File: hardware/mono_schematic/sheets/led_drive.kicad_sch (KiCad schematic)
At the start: 31 parts

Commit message: mono_electronics v11b: TLV75733P 1A AON LDO, 22uF ESP32 bulk, LED_EN RC glitch filter, J_USB value, refs end in digit; schematic regenerated (ERC 0, 0 diffs)
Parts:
- removed C_BUF_V, C_DECA_V, C_DECB_V, C_LED1_V, C_LED2_V, C_XLAT_A, C_XLAT_B: 100n, mono_electronics:C_0402_1005Metric, symbol mono_parts:100n_C_0402_1005Metric_2
- removed J_COL: FFC_40P_050_COL, mono_electronics:FFC_40P_050_COL, symbol mono_parts:FFC_40P_050_COL_FFC_40P_050_COL_40
- removed R_CLK_PD, R_LE_PD, R_SDI_PD: 100k, mono_electronics:R_0402_1005Metric, symbol mono_parts:100k_R_0402_1005Metric_2
- removed R_CLK_SER, R_LE_SER, R_SDI_SER: 22R, mono_electronics:R_0402_1005Metric, symbol mono_parts:22R_R_0402_1005Metric_2
- removed R_ENA, R_ENB, R_OE_PU, R_OE_YPU: 47k, mono_electronics:R_0402_1005Metric, symbol mono_parts:47k_R_0402_1005Metric_2
- removed R_XOE: 10k, mono_electronics:R_0402_1005Metric, symbol mono_parts:10k_R_0402_1005Metric_2
- removed U_DEC_A, U_DEC_B: 74HC154, mono_electronics:TSSOP-24_4.4x7.8mm_P0.65mm, symbol mono_parts:74HC154_TSSOP-24_4.4x7.8mm_P0.65mm_24
- removed U_LED_BUF: SN74LV125A, mono_electronics:TSSOP-14_4.4x5mm_P0.65mm, symbol mono_parts:SN74LV125A_TSSOP-14_4.4x5mm_P0.65mm_14
- removed U_ROW_XLAT: SN74LVC8T245RHLR, mono_electronics:Texas_RHL0024A_VQFN-24-1EP_3.5x5.5mm_P0.5mm_EP2.05x4.05mm, symbol mono_parts:SN74LVC8T245RHLR_Texas_RHL0024A_VQFN-24-1EP_3.5x5.5mm_P0.5mm_EP2.05x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
- added C_BUF_V1, C_DECA_V1, C_DECB_V1, C_LED1_V1, C_LED2_V1, C_XLAT_A1, C_XLAT_B1: 100n, mono_electronics:C_0402_1005Metric, symbol mono_parts:100n_C_0402_1005Metric_2
- added J_COL1: FFC_40P_050_COL, mono_electronics:FFC_40P_050_COL, symbol mono_parts:FFC_40P_050_COL_FFC_40P_050_COL_40
- added R_CLK_PD1, R_EN_PD1, R_EN_SER1, R_LE_PD1, R_SDI_PD1: 100k, mono_electronics:R_0402_1005Metric, symbol mono_parts:100k_R_0402_1005Metric_2
- added R_CLK_SER1, R_LE_SER1, R_SDI_SER1: 22R, mono_electronics:R_0402_1005Metric, symbol mono_parts:22R_R_0402_1005Metric_2
- added R_ENA1, R_ENB1, R_OE_PU1, R_OE_YPU1: 47k, mono_electronics:R_0402_1005Metric, symbol mono_parts:47k_R_0402_1005Metric_2
- added R_XOE1: 10k, mono_electronics:R_0402_1005Metric, symbol mono_parts:10k_R_0402_1005Metric_2
- added U_DEC_A1, U_DEC_B1: 74HC154, mono_electronics:TSSOP-24_4.4x7.8mm_P0.65mm, symbol mono_parts:74HC154_TSSOP-24_4.4x7.8mm_P0.65mm_24
- added U_LED_BUF1: SN74LV125A, mono_electronics:TSSOP-14_4.4x5mm_P0.65mm, symbol mono_parts:SN74LV125A_TSSOP-14_4.4x5mm_P0.65mm_14
- added U_LED_LOGIC1: TPS22917, mono_electronics:SOT-23-6, symbol mono_parts:TPS22917_SOT-23-6_5
- added U_LED_PWR1: TPS63802DLAR, mono_electronics:TDFN-10-1EP_2x3mm_P0.5mm_EP0.9x2mm, symbol mono_parts:TPS63802DLAR_TDFN-10-1EP_2x3mm_P0.5mm_EP0.9x2mm_10
- added U_ROW_XLAT1: SN74LVC8T245RHLR, mono_electronics:Texas_RHL0024A_VQFN-24-1EP_3.5x5.5mm_P0.5mm_EP2.05x4.05mm, symbol mono_parts:SN74LVC8T245RHLR_Texas_RHL0024A_VQFN-24-1EP_3.5x5.5mm_P0.5mm_EP2.05x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
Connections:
- net AON_3V3: now also C_XLAT_A1.1, R_OE_PU1.2, R_XOE1.1, U_LED_LOGIC1.1 (AON_3V3), U_ROW_XLAT1.1 (AON_3V3), U_ROW_XLAT1.2 (AON_3V3)
- net COL_01: now also J_COL1.1 (COL_01)
- net COL_02: now also J_COL1.2 (COL_02)
- net COL_03: now also J_COL1.3 (COL_03)
- net COL_04: now also J_COL1.4 (COL_04)
- net COL_05: now also J_COL1.5 (COL_05)
- net COL_06: now also J_COL1.6 (COL_06)
- net COL_07: now also J_COL1.7 (COL_07)
- net COL_08: now also J_COL1.8 (COL_08)
- net COL_09: now also J_COL1.9 (COL_09)
- net COL_10: now also J_COL1.10 (COL_10)
- net COL_11: now also J_COL1.11 (COL_11)
- net COL_12: now also J_COL1.12 (COL_12)
- net COL_13: now also J_COL1.13 (COL_13)
- net COL_14: now also J_COL1.14 (COL_14)
- net COL_15: now also J_COL1.15 (COL_15)
- net COL_16: now also J_COL1.16 (COL_16)
- net COL_17: now also J_COL1.17 (COL_17)
- net COL_18: now also J_COL1.18 (COL_18)
- net COL_19: now also J_COL1.19 (COL_19)
- net COL_20: now also J_COL1.20 (COL_20)
- net COL_21: now also J_COL1.21 (COL_21)
- net COL_22: now also J_COL1.22 (COL_22)
- net COL_23: now also J_COL1.23 (COL_23)
- net COL_24: now also J_COL1.24 (COL_24)
- net COL_25: now also J_COL1.25 (COL_25)
- net COL_26: now also J_COL1.26 (COL_26)
- net COL_27: now also J_COL1.27 (COL_27)
- net COL_28: now also J_COL1.28 (COL_28)
- net COL_29: now also J_COL1.29 (COL_29)
- net COL_30: now also J_COL1.30 (COL_30)
- net COL_31: now also J_COL1.31 (COL_31)
- net COL_32: now also J_COL1.32 (COL_32)
- net DEC_A_EN_N: now also U_ROW_XLAT1.7 (DEC_A_EN_N)
- net DEC_A_EN_N_4V: now also R_ENA1.1, U_DEC_A1.18 (DEC_A_EN_N_4V), U_ROW_XLAT1.17 (DEC_A_EN_N_4V)
- net DEC_B_EN_N: now also U_ROW_XLAT1.8 (DEC_B_EN_N)
- net DEC_B_EN_N_4V: now also R_ENB1.1, U_DEC_B1.18 (DEC_A_EN_N_4V), U_ROW_XLAT1.16 (DEC_B_EN_N_4V)
- net GND: now also C_BUF_V1.2, C_DECA_V1.2, C_DECB_V1.2, C_LED1_V1.2, C_LED2_V1.2, C_XLAT_A1.2, C_XLAT_B1.2, R_CLK_PD1.2, R_EN_PD1.2, R_LE_PD1.2, R_SDI_PD1.2, U_DEC_A1.12 (GND), U_DEC_A1.19 (GND), U_DEC_B1.12 (GND), U_DEC_B1.19 (GND), U_LED_BUF1.1 (GND), U_LED_BUF1.10 (GND), U_LED_BUF1.13 (GND), U_LED_BUF1.4 (GND), U_LED_BUF1.7 (GND), U_LED_LOGIC1.2 (GND), U_LED_PWR1.11 (GND), U_LED_PWR1.2 (GND), U_LED_PWR1.3 (GND), U_LED_PWR1.8 (GND), U_ROW_XLAT1.10 (GND), U_ROW_XLAT1.11 (GND), U_ROW_XLAT1.12 (GND), U_ROW_XLAT1.13 (GND), U_ROW_XLAT1.25 (GND), U_ROW_XLAT1.9 (GND)
- net LED_4V1: now also C_DECA_V1.1, C_DECB_V1.1, C_XLAT_B1.1, R_ENA1.2, R_ENB1.2, U_DEC_A1.24 (LED_4V1), U_DEC_B1.24 (LED_4V1), U_LED_PWR1.6 (LED_4V1), U_ROW_XLAT1.23 (LED_4V1), U_ROW_XLAT1.24 (LED_4V1)
- net LED_CLK: now also R_CLK_PD1.1, U_LED_BUF1.2 (LED_CLK)
- net LED_CLK_PRE: now also R_CLK_SER1.1, U_LED_BUF1.3 (LED_CLK_PRE)
- net LED_CLK_Y: now also R_CLK_SER1.2
- net LED_LE: now also R_LE_PD1.1, U_LED_BUF1.9 (LED_LE)
- net LED_LE_PRE: now also R_LE_SER1.1, U_LED_BUF1.8 (LED_LE_PRE)
- net LED_LE_Y: now also R_LE_SER1.2
- net LED_LOGIC_3V3: now also C_BUF_V1.1, C_LED1_V1.1, C_LED2_V1.1, R_OE_YPU1.2, U_LED_BUF1.14 (LED_LOGIC_3V3), U_LED_LOGIC1.6 (LED_LOGIC_3V3)
- net LED_OE_N: now also R_OE_PU1.1, U_LED_BUF1.12 (LED_OE_N)
- net LED_OE_Y: now also R_OE_YPU1.1, U_LED_BUF1.11 (LED_OE_Y)
- net LED_SDI: now also R_SDI_PD1.1, U_LED_BUF1.5 (LED_SDI)
- net LED_SDI_PRE: now also R_SDI_SER1.1, U_LED_BUF1.6 (LED_SDI_PRE)
- net LED_SDI_Y: now also R_SDI_SER1.2
- net ROW_01_Y: now also U_DEC_A1.1 (ROW_01_Y)
- net ROW_02_Y: now also U_DEC_A1.2 (ROW_02_Y)
- net ROW_03_Y: now also U_DEC_A1.3 (ROW_03_Y)
- net ROW_04_Y: now also U_DEC_A1.4 (ROW_04_Y)
- net ROW_05_Y: now also U_DEC_A1.5 (ROW_05_Y)
- net ROW_06_Y: now also U_DEC_A1.6 (ROW_06_Y)
- net ROW_07_Y: now also U_DEC_A1.7 (ROW_07_Y)
- net ROW_08_Y: now also U_DEC_A1.8 (ROW_08_Y)
- net ROW_09_Y: now also U_DEC_A1.9 (ROW_09_Y)
- net ROW_10_Y: now also U_DEC_A1.10 (ROW_10_Y)
- net ROW_11_Y: now also U_DEC_A1.11 (ROW_11_Y)
- net ROW_12_Y: now also U_DEC_A1.13 (ROW_12_Y)
- net ROW_13_Y: now also U_DEC_A1.14 (ROW_13_Y)
- net ROW_14_Y: now also U_DEC_A1.15 (ROW_14_Y)
- net ROW_15_Y: now also U_DEC_A1.16 (ROW_15_Y)
- net ROW_16_Y: now also U_DEC_A1.17 (ROW_16_Y)
- net ROW_17_Y: now also U_DEC_B1.1 (ROW_01_Y)
- net ROW_18_Y: now also U_DEC_B1.2 (ROW_02_Y)
- net ROW_19_Y: now also U_DEC_B1.3 (ROW_03_Y)
- net ROW_20_Y: now also U_DEC_B1.4 (ROW_04_Y)
- net ROW_21_Y: now also U_DEC_B1.5 (ROW_05_Y)
- net ROW_22_Y: now also U_DEC_B1.6 (ROW_06_Y)
- net ROW_23_Y: now also U_DEC_B1.7 (ROW_07_Y)
- net ROW_24_Y: now also U_DEC_B1.8 (ROW_08_Y)
- net ROW_25_Y: now also U_DEC_B1.9 (ROW_09_Y)
- net ROW_26_Y: now also U_DEC_B1.10 (ROW_10_Y)
- net ROW_27_Y: now also U_DEC_B1.11 (ROW_11_Y)
- net ROW_28_Y: now also U_DEC_B1.13 (ROW_12_Y)
- net ROW_29_Y: now also U_DEC_B1.14 (ROW_13_Y)
- net ROW_30_Y: now also U_DEC_B1.15 (ROW_14_Y)
- net ROW_31_Y: now also U_DEC_B1.16 (ROW_15_Y)
- net ROW_32_Y: now also U_DEC_B1.17 (ROW_16_Y)
- net ROW_A0: now also U_ROW_XLAT1.3 (ROW_A0)
- net ROW_A0_4V: now also U_DEC_A1.23 (ROW_A0_4V), U_DEC_B1.23 (ROW_A0_4V), U_ROW_XLAT1.21 (ROW_A0_4V)
- net ROW_A1: now also U_ROW_XLAT1.4 (ROW_A1)
- net ROW_A1_4V: now also U_DEC_A1.22 (ROW_A1_4V), U_DEC_B1.22 (ROW_A1_4V), U_ROW_XLAT1.20 (ROW_A1_4V)
- net ROW_A2: now also U_ROW_XLAT1.5 (ROW_A2)
- net ROW_A2_4V: now also U_DEC_A1.21 (ROW_A2_4V), U_DEC_B1.21 (ROW_A2_4V), U_ROW_XLAT1.19 (ROW_A2_4V)
- net ROW_A3: now also U_ROW_XLAT1.6 (ROW_A3)
- net ROW_A3_4V: now also U_DEC_A1.20 (ROW_A3_4V), U_DEC_B1.20 (ROW_A3_4V), U_ROW_XLAT1.18 (ROW_A3_4V)
- net ROW_XLAT_OE_N: now also R_XOE1.2, U_ROW_XLAT1.22 (ROW_XLAT_OE_N)
- new net LED_EN: R_EN_PD1.1, R_EN_SER1.1
- new net LED_EN_RC: R_EN_SER1.2, U_LED_PWR1.1 (LED_EN_RC)
- new net LED_FB: U_LED_PWR1.4 (LED_FB)
- new net LED_LOGIC_EN: U_LED_LOGIC1.3 (LED_LOGIC_EN)
- new net LED_QOD: U_LED_LOGIC1.5 (LED_QOD)
- new net SW_L1: U_LED_PWR1.9 (SW_L1)
- new net SW_L2: U_LED_PWR1.7 (SW_L2)
- new net SYS: U_LED_PWR1.10 (SYS)

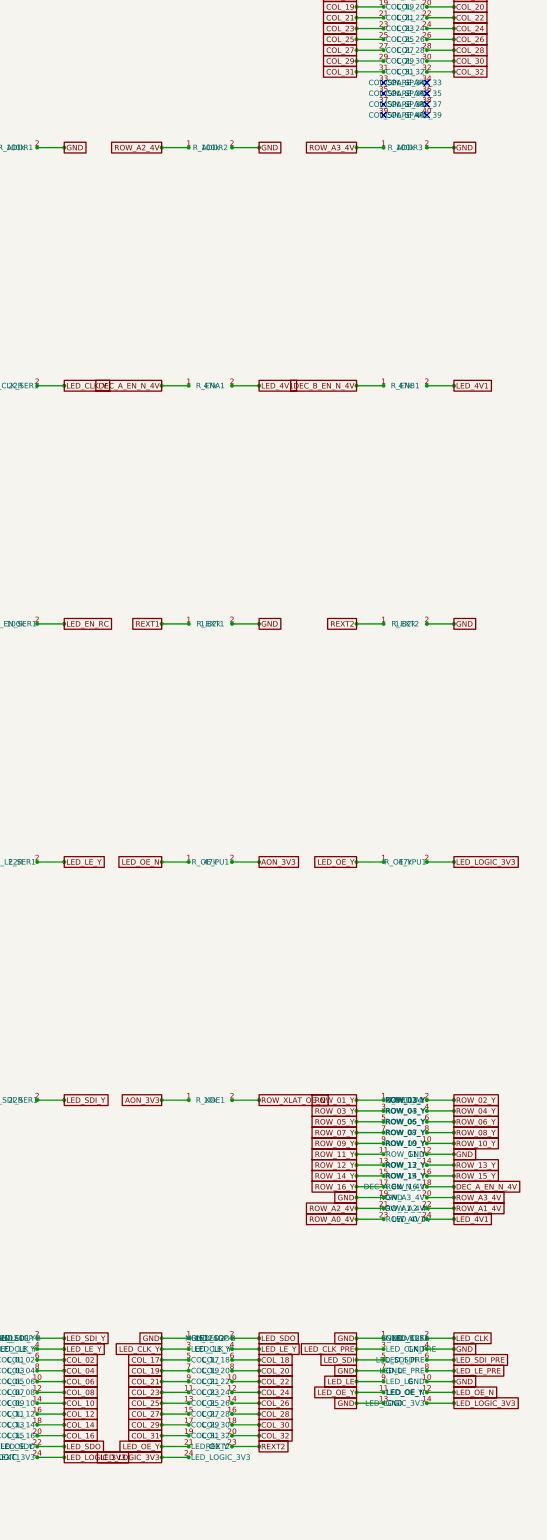
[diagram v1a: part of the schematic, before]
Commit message: mono_electronics v12: LED interface standard on FFC spares (ID I2C 33R+PESD5V0S2BT, ID_3V3 100R, GND 33/38/40; DNP column-expansion taps incl. U_LED2 SDO), schematic regen (ERC 0, 0 diffs), fab v12; garland 480 Hz scan mode (scan_div) + timing fix
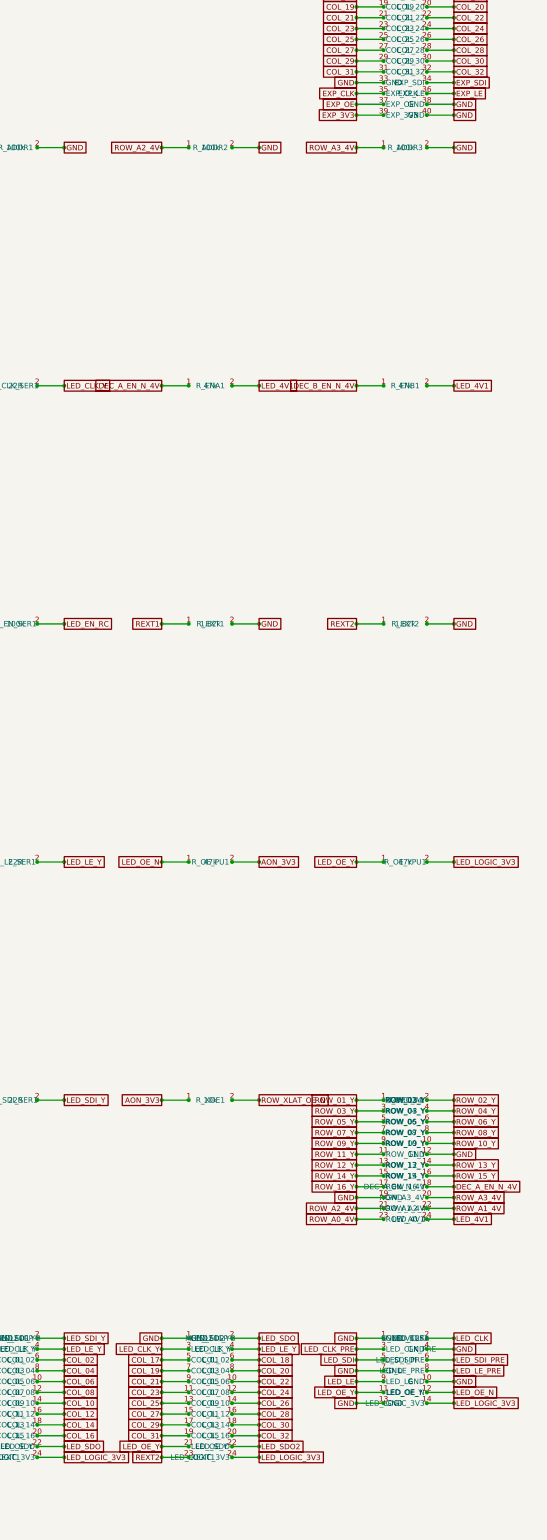
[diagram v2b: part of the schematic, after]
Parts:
- removed U_LED2: MBI5124GP-B, mono_electronics:SSOP-24_3.9x8.7mm_P0.635mm, symbol mono_parts:MBI5124GP-B_SSOP-24_3.9x8.7mm_P0.635mm_23
- added U_LED2: MBI5124GP-B, mono_electronics:SSOP-24_3.9x8.7mm_P0.635mm, symbol mono_parts:MBI5124GP-B_SSOP-24_3.9x8.7mm_P0.635mm_24
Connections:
- net COL_17: now also U_LED2.5 (COL_01)
- net COL_18: now also U_LED2.6 (COL_02)
- net COL_19: now also U_LED2.7 (COL_03)
- net COL_20: now also U_LED2.8 (COL_04)
- net COL_21: now also U_LED2.9 (COL_05)
- net COL_22: now also U_LED2.10 (COL_06)
- net COL_23: now also U_LED2.11 (COL_07)
- net COL_24: now also U_LED2.12 (COL_08)
- net COL_25: now also U_LED2.13 (COL_09)
- net COL_26: now also U_LED2.14 (COL_10)
- net COL_27: now also U_LED2.15 (COL_11)
- net COL_28: now also U_LED2.16 (COL_12)
- net COL_29: now also U_LED2.17 (COL_13)
- net COL_30: now also U_LED2.18 (COL_14)
- net COL_31: now also U_LED2.19 (COL_15)
- net COL_32: now also U_LED2.20 (COL_16)
- net GND: now also J_COL1.33 (GND), J_COL1.38 (GND), J_COL1.40 (GND), U_LED2.1 (GND)
- net LED_CLK_Y: now also U_LED2.3 (LED_CLK_Y)
- net LED_LE_Y: now also U_LED2.4 (LED_LE_Y)
- net LED_LOGIC_3V3: now also U_LED2.24 (LED_LOGIC_3V3)
- net LED_OE_Y: now also U_LED2.21 (LED_OE_Y)
- net LED_SDO: now also U_LED2.2 (LED_SDI_Y)
- net REXT2: now also U_LED2.23 (REXT1)
- net EXP_SDI: now reaches J_COL1.34 (EXP_SDI)
- net EXP_CLK: now reaches J_COL1.35 (EXP_CLK)
- net EXP_LE: now reaches J_COL1.36 (EXP_LE)
- net EXP_OE: now reaches J_COL1.37 (EXP_OE)
- net EXP_3V3: now reaches J_COL1.39 (EXP_3V3)
- new net LED_SDO2: U_LED2.22 (LED_SDO)
- no-connect marks 8 -> 0

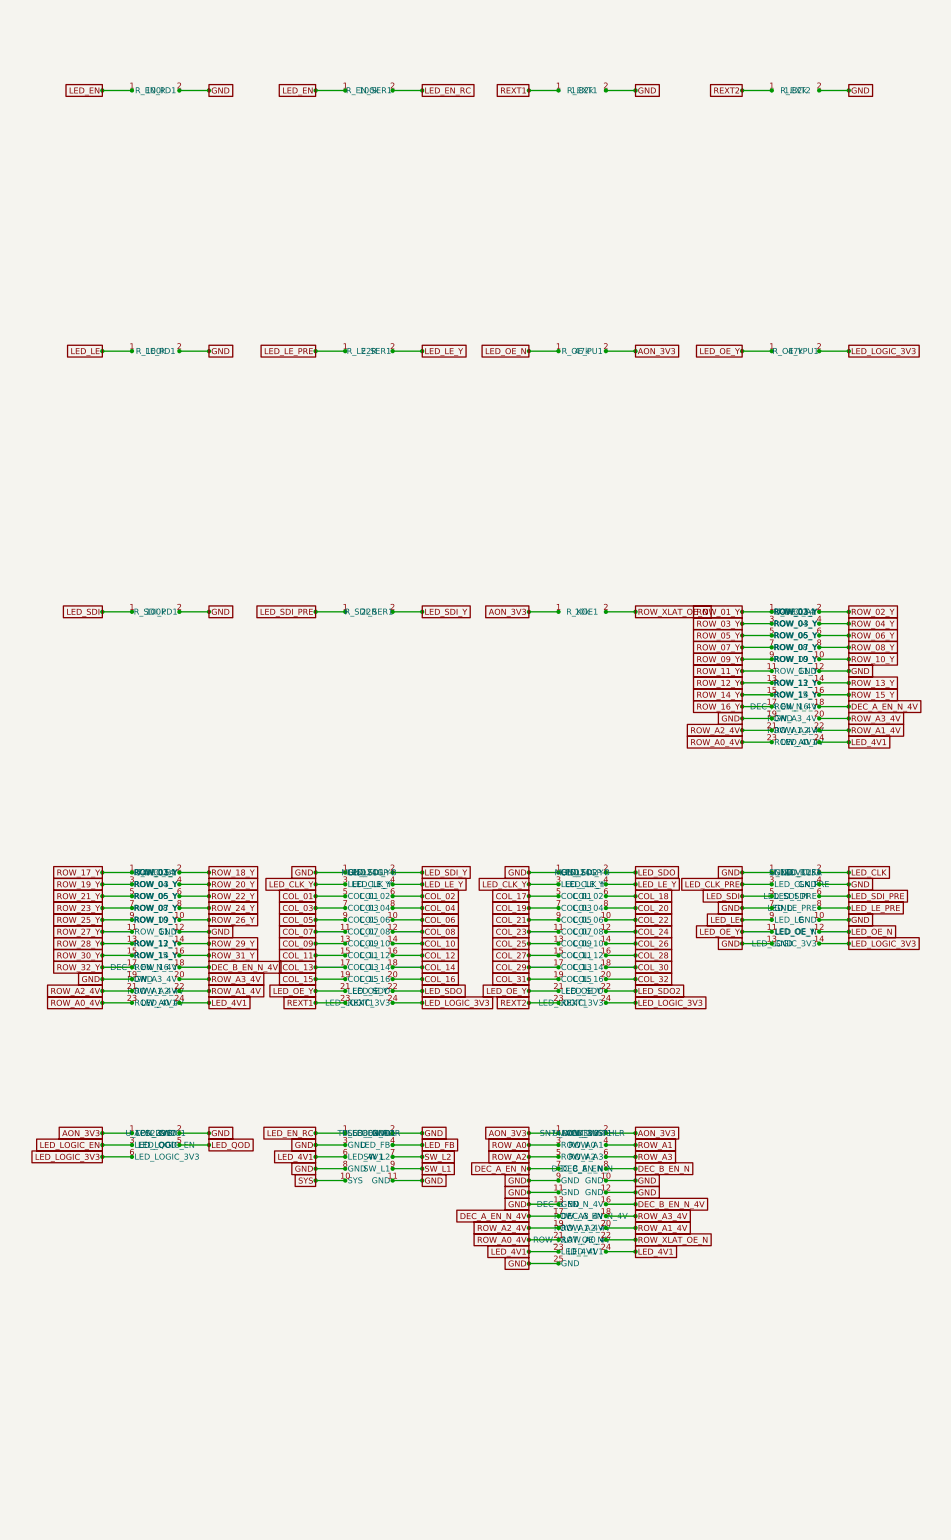
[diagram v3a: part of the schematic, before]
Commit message: mono_electronics v13 chunk2: USB input OVP — U_OVP1 TPS259531DSGR eFuse (5.7 V OV clamp, 1.17 A limit R_ILM1 1.78k, UVLO 4.28 V via 100k/39k), D_VBUS1 SMF12A TVS on VBUS_CONN; USBLC6 now on protected VBUS; schematic regen (ERC 0, 0 diffs); DRC 0/0/0
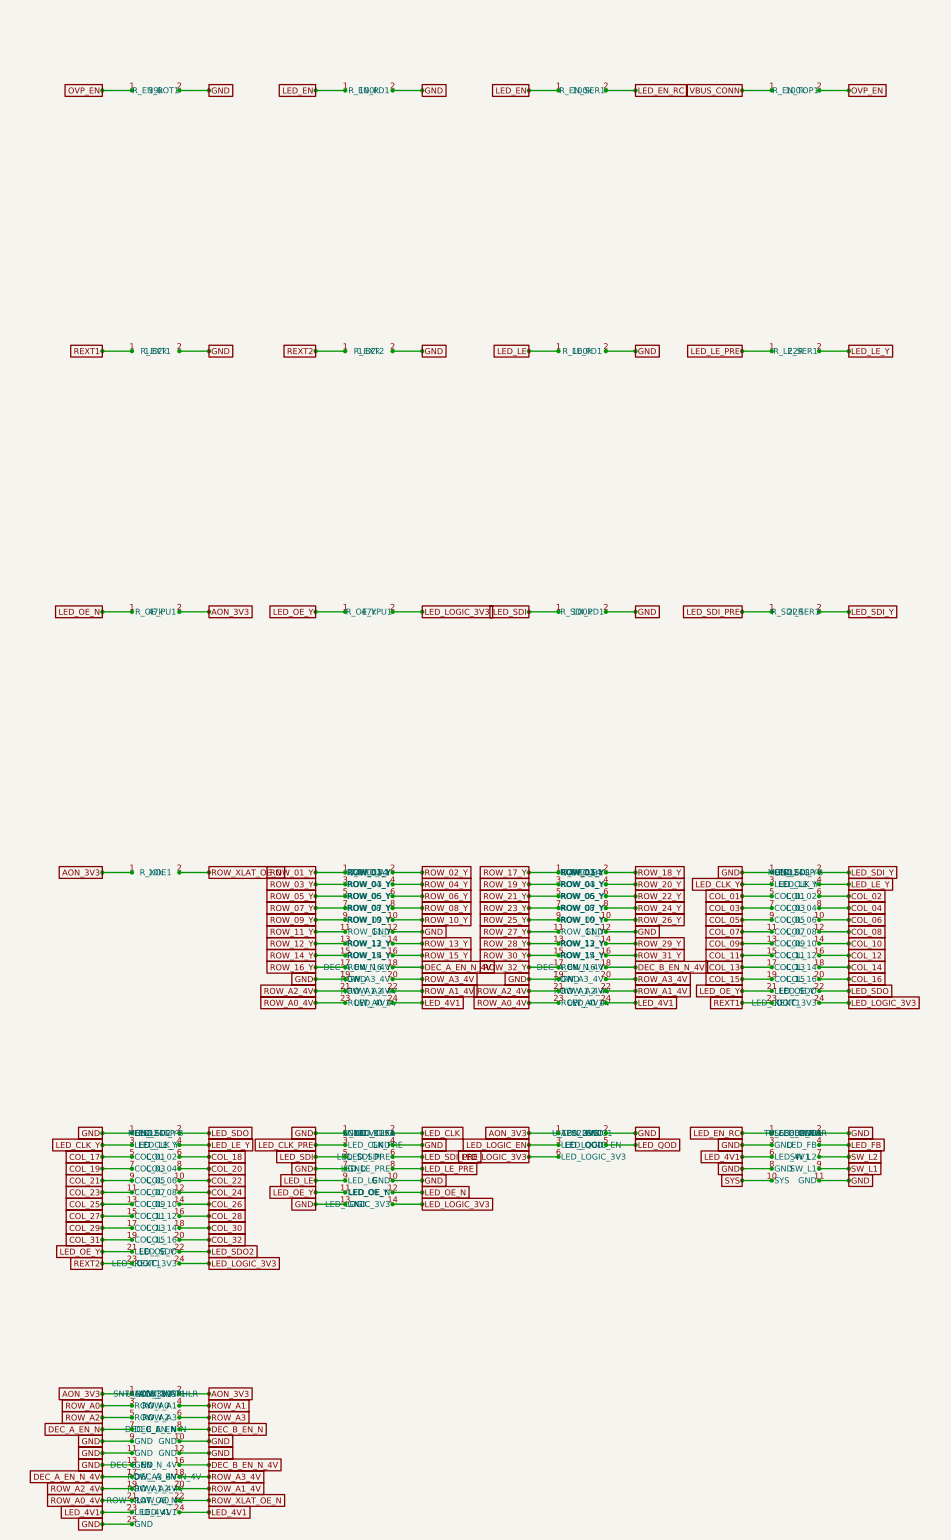
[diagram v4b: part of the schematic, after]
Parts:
- added R_EN_BOT1: 39k, mono_electronics:R_0402_1005Metric, symbol mono_parts:39k_R_0402_1005Metric_2
- added R_EN_TOP1: 100k, mono_electronics:R_0402_1005Metric, symbol mono_parts:100k_R_0402_1005Metric_2
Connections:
- net GND: now also R_EN_BOT1.2
- new net OVP_EN: R_EN_BOT1.1, R_EN_TOP1.2
- new net VBUS_CONN: R_EN_TOP1.1
